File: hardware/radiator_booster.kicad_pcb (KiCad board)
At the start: 4 copper layers, 40 x 40 mm, 56 parts, among them J301 USB_C_Receptacle_USB2.0, J401 Fan1, J402 Fan2, J403 Fan3, J404 Fan4, J405 Fan5, SW301 RESET, SW302 BOOT, U201 SPX3819M5-L-3-3, U301 USBLC6-2SC6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

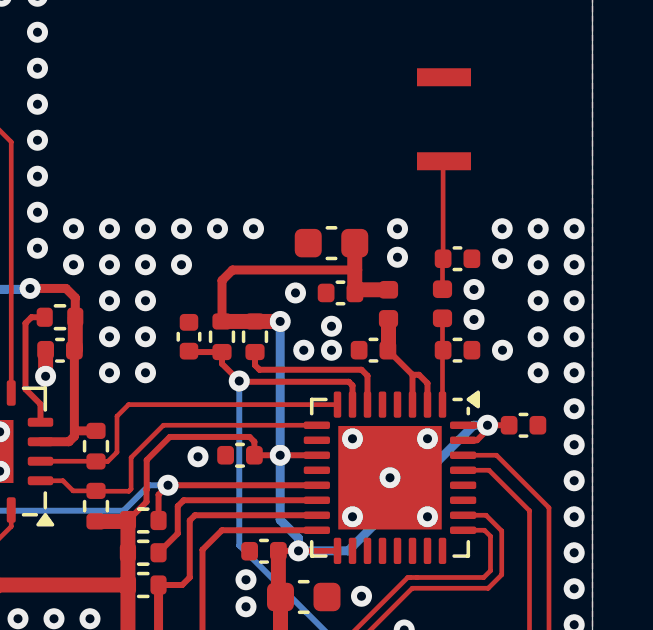
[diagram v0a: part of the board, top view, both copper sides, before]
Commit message: Updated matching network. Changed inductor for all filter for bom sonsolidation after matching network changes
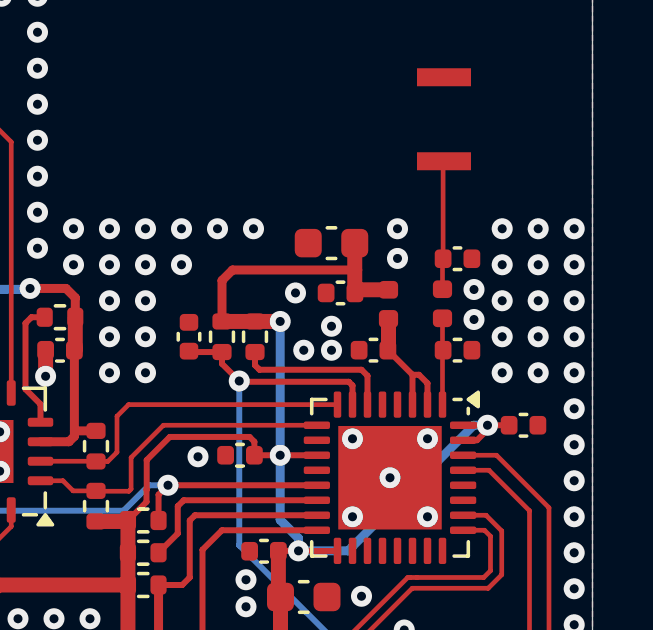
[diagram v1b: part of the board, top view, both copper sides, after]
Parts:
- L201, L301, L302: value 2n2 -> 2n3
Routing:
- net GND: vias 212 -> 214
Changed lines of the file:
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@@
 			)
 		)
-		(property "Value" "2n2"
+		(property "Value" "2n3"
 			(at 0 1.17 90)
 			(layer "F.Fab")
@@
 			)
 		)
-		(property "Rating" "2.53A"
+		(property "Rating" "1A"
 			(at 0 0 270)
 			(unlocked yes)
@@
 			)
 		)
-		(property "MPN" "C412264"
+		(property "MPN" "C412340"
 			(at 0 0 270)
 			(unlocked yes)
@@
 			)
 		)
-		(property "Value" "2n2"
+		(property "Value" "2n3"
 			(at 0 1.17 90)
 			(layer "F.Fab")
@@
 			)
 		)
-		(property "Rating" "2.53A"
+		(property "Rating" "1A"
 			(at 0 0 270)
 			(unlocked yes)
@@
 			)
 		)
-		(property "MPN" "C412264"
+		(property "MPN" "C412340"
 			(at 0 0 270)
 			(unlocked yes)
@@
 			)
 		)
-		(property "Value" "2n2"
+		(property "Value" "2n3"
 			(at 0 1.17 0)
 			(layer "F.Fab")
@@
 			)
 		)
-		(property "Rating" "2.53A"
+		(property "Rating" "1A"
 			(at 0 0 180)
 			(unlocked yes)
@@
 			)
 		)
-		(property "MPN" "C412264"
+		(property "MPN" "C412340"
 			(at 0 0 180)
 			(unlocked yes)
@@
 			)
 		)
-		(property "MPN" "C1564"
+		(property "MPN" "C88891"
 			(at 0 0 0)
 			(unlocked yes)
@@
 			)
 		)
-		(property "MPN" "C1564"
+		(property "MPN" "C88891"
 			(at 0 0 0)
 			(unlocked yes)
@@
 	)
 	(via
+		(at 173.99 77.3)
+		(size 0.7)
+		(drill 0.3)
+		(layers "F.Cu" "B.Cu")
+		(free yes)
+		(net 1)
+	)
+	(via
 		(at 151.300003 75.05)
 		(size 0.7)
@@
 	)
 	(via
-		(at 174 73.5)
-		(size 0.7)
-		(drill 0.3)
-		(layers "F.Cu" "B.Cu")
-		(free yes)
-		(net 1)
-	)
-	(via
 		(at 138.1 79.15)
 		(size 0.7)
@@
 	)
 	(via
+		(at 173.99 74.9)
+		(size 0.7)
+		(drill 0.3)
+		(layers "F.Cu" "B.Cu")
+		(free yes)
+		(net 1)
+	)
+	(via
 		(at 138.1 93.55)
 		(size 0.7)
@@
 	)
 	(via
-		(at 174 76.55)
-		(size 0.7)
-		(drill 0.3)
-		(layers "F.Cu" "B.Cu")
-		(free yes)
-		(net 1)
-	)
-	(via
 		(at 139.3 103.36)
 		(size 0.7)
@@
 	)
 	(via
+		(at 173.99 76.1)
+		(size 0.7)
+		(drill 0.3)
+		(layers "F.Cu" "B.Cu")
+		(free yes)
+		(net 1)
+	)
+	(via
 		(at 170.3 91.225)
 		(size 0.7)
@@
 	)
 	(via
+		(at 173.99 73.7)
+		(size 0.7)
+		(drill 0.3)
+		(layers "F.Cu" "B.Cu")
+		(free yes)
+		(net 1)
+	)
+	(via
 		(at 157.85 86.5)
 		(size 0.7)
@@
 	)
 	(via
-		(at 170.5 73.45)
+		(at 170.5 73.49)
 		(size 0.7)
 		(drill 0.3)
@@
 		(polygon
 			(pts
-				(xy 150.119535 67.984292) (xy 149.978148 86.855477) (xy 156.07 86.14) (xy 156.9 67.99)
+				(xy 150.119535 67.984292) (xy 149.978148 86.855477) (xy 155.9 86.43) (xy 156.15 68.01)
 			)
 		)
